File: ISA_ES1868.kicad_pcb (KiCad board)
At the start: 4 copper layers, 104.1 x 99.1 mm, 105 parts, among them J1 LINE IN, J10 Volume buttons, J11 ISA BUS, J2 MIC, J3 Joystick/MIDI, J5 Wavetable, J7 SPKR OUT, J8 LINE OUT, U1 L78L05, U2 74LS138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

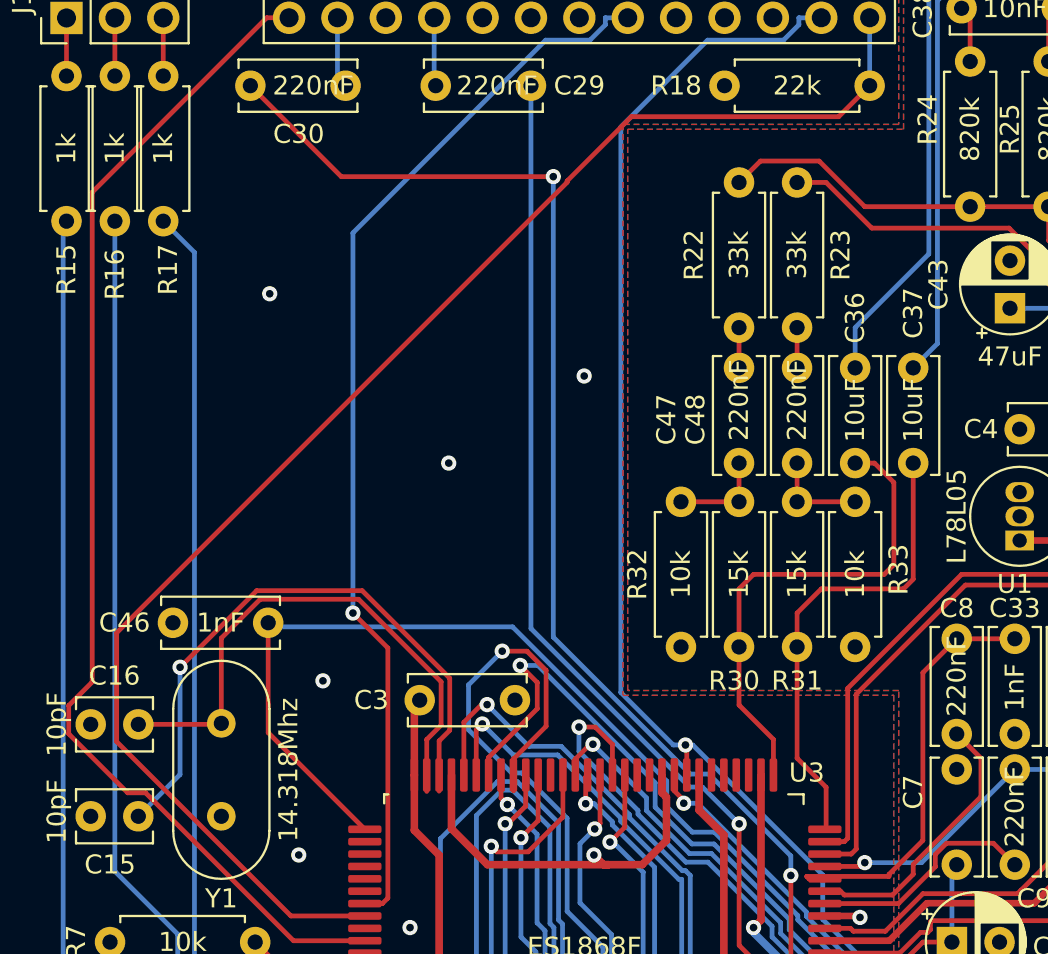
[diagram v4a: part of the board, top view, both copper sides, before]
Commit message: Changed some routing
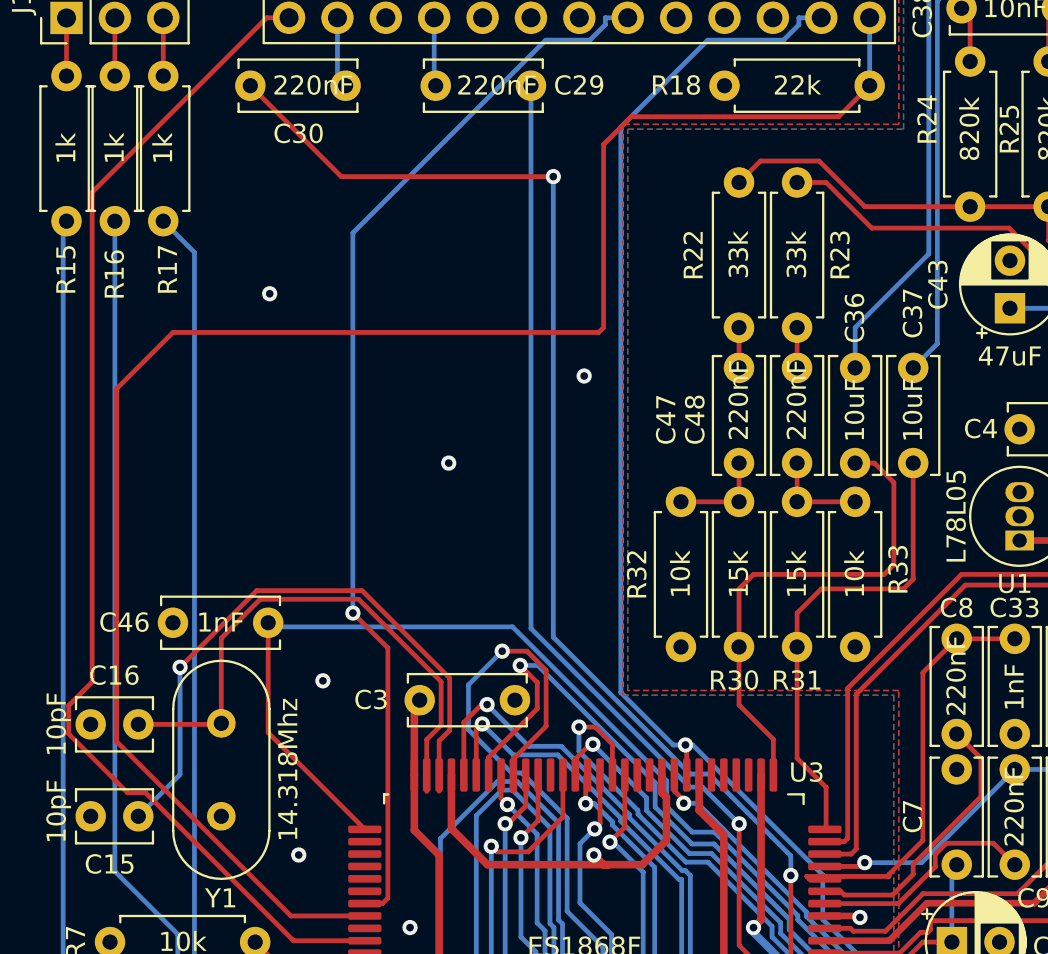
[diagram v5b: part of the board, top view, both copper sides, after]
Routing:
- net /MCLK: track 77.6 -> 90.7 mm
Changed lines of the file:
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@@
     (thickness 1.6)
     (drawings 14)
-    (tracks 1333)
+    (tracks 1336)
     (zones 0)
     (modules 105)
@@
     (tags "solder jumper open")
     (attr virtual)
-    (fp_text reference JP6 (at 0 -2.032 270) (layer B.SilkS)
+    (fp_text reference JP6 (at -2.27 0.254 180) (layer B.SilkS)
       (effects (font (size 1 1) (thickness 0.15)) (justify mirror))
     )
@@
     (tags "solder jumper open")
     (attr virtual)
-    (fp_text reference JP4 (at 0 1.778 270) (layer B.SilkS)
+    (fp_text reference JP4 (at -2.27 0 180) (layer B.SilkS)
       (effects (font (size 1 1) (thickness 0.15)) (justify mirror))
     )
@@
     (descr "C, Disc series, Radial, pin pitch=5.00mm, , diameter*width=6*2.5mm^2, Capacitor, http://cdn-reichelt.de/documents/datenblatt/B300/DS_KERKO_TC.pdf")
     (tags "C Disc series Radial pin pitch 5.00mm  diameter 6mm width 2.5mm Capacitor")
-    (fp_text reference C7 (at 3.81 -2.286 90) (layer F.SilkS)
+    (fp_text reference C7 (at 2.54 -2.286 90) (layer F.SilkS)
       (effects (font (size 1 1) (thickness 0.15)))
     )
@@
   (segment (start 254.508 108.956) (end 253.3327 108.956) (width 0.25) (layer B.Cu) (net 54))
   (via (at 247.377 147.1322) (size 0.8) (layers F.Cu B.Cu) (net 54))
-  (segment (start 230.545 156.109) (end 226.6705 156.109) (width 0.25) (layer F.Cu) (net 55))
-  (segment (start 226.6705 156.109) (end 217.518 146.9565) (width 0.25) (layer F.Cu) (net 55))
-  (segment (start 217.518 146.9565) (end 217.518 141.2428) (width 0.25) (layer F.Cu) (net 55))
-  (segment (start 217.518 141.2428) (end 241.1651 117.5957) (width 0.25) (layer F.Cu) (net 55))
-  (segment (start 241.1651 117.5957) (end 241.1651 117.5247) (width 0.25) (layer F.Cu) (net 55))
-  (segment (start 241.1651 117.5247) (end 244.5423 114.1475) (width 0.25) (layer F.Cu) (net 55))
   (segment (start 244.5423 114.1475) (end 255.4225 114.1475) (width 0.25) (layer F.Cu) (net 55))
   (segment (start 255.4225 114.1475) (end 257.048 112.522) (width 0.25) (layer F.Cu) (net 55))
   (segment (start 257.048 108.956) (end 257.048 112.522) (width 0.25) (layer B.Cu) (net 55))
+  (segment (start 243.078 115.6118) (end 243.0989 115.5909) (width 0.25) (layer F.Cu) (net 55))
+  (segment (start 243.078 125.222) (end 243.078 115.6118) (width 0.25) (layer F.Cu) (net 55))
+  (segment (start 242.824 125.476) (end 243.078 125.222) (width 0.25) (layer F.Cu) (net 55))
+  (segment (start 220.472 125.476) (end 242.824 125.476) (width 0.25) (layer F.Cu) (net 55))
+  (segment (start 217.518 128.43) (end 220.472 125.476) (width 0.25) (layer F.Cu) (net 55))
+  (segment (start 226.6705 156.109) (end 217.518 146.9565) (width 0.25) (layer F.Cu) (net 55))
+  (segment (start 230.545 156.109) (end 226.6705 156.109) (width 0.25) (layer F.Cu) (net 55))
+  (segment (start 217.518 146.9565) (end 217.518 128.43) (width 0.25) (layer F.Cu) (net 55))
+  (segment (start 243.0989 115.5909) (end 244.5423 114.1475) (width 0.25) (layer F.Cu) (net 55))
   (segment (start 219.964 108.966) (end 219.964 112.014) (width 0.25) (layer F.Cu) (net 56))
   (segment (start 217.424 108.966) (end 217.424 112.014) (width 0.25) (layer F.Cu) (net 57))

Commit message: Change silkscreen
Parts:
- J10: value Volume buttons -> Vol. Btns
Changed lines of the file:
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@@
   (page A3)
   (layers
-    (0 F.Cu signal)
-    (1 In1.Cu power)
-    (2 In2.Cu power)
-    (31 B.Cu signal)
+    (0 F.Cu signal hide)
+    (1 In1.Cu power hide)
+    (2 In2.Cu power hide)
+    (31 B.Cu signal hide)
     (32 B.Adhes user)
     (33 F.Adhes user)
@@
       (effects (font (size 1 1) (thickness 0.15)))
     )
-    (fp_text value "LINE OUT" (at 4.385 7.35 90) (layer F.Fab)
+    (fp_text value "LINE OUT" (at -2.6 2.54) (layer F.SilkS)
       (effects (font (size 1 1) (thickness 0.15)))
     )
@@
       (effects (font (size 1 1) (thickness 0.15)))
     )
-    (fp_text value 100nF (at 2.5 2.5) (layer F.Fab)
+    (fp_text value 100nF (at 3.048 0) (layer F.SilkS)
       (effects (font (size 1 1) (thickness 0.15)))
     )
@@
     (descr "Resistor, Axial_DIN0207 series, Axial, Horizontal, pin pitch=7.62mm, 0.25W = 1/4W, length*diameter=6.3*2.5mm^2, http://cdn-reichelt.de/documents/datenblatt/B400/1_4W%23YAG.pdf")
     (tags "Resistor Axial_DIN0207 series Axial Horizontal pin pitch 7.62mm 0.25W = 1/4W length 6.3mm diameter 2.5mm")
-    (fp_text reference R18 (at 10.16 0) (layer F.SilkS)
+    (fp_text reference R18 (at 4.064 -2.286) (layer F.SilkS)
       (effects (font (size 1 1) (thickness 0.15)))
     )
@@
       (effects (font (size 1 1) (thickness 0.15)))
     )
-    (fp_text value "Volume buttons" (at 1.27 7.41 90) (layer F.Fab)
+    (fp_text value "Vol. Btns" (at 1.27 7.41 90) (layer F.SilkS)
       (effects (font (size 1 1) (thickness 0.15)))
     )
@@
       (effects (font (size 1 1) (thickness 0.15)))
     )
-    (fp_text value Wavetable (at 1.27 32.81 90) (layer F.Fab)
+    (fp_text value Wavetable (at 5.344 12.446) (layer F.SilkS)
       (effects (font (size 1 1) (thickness 0.15)))
     )
@@
       (effects (font (size 1 1) (thickness 0.15)))
     )
-    (fp_text value Joystick/MIDI (at -9.695 15.85 90) (layer F.Fab)
+    (fp_text value Joystick/MIDI (at -10.668 6.096 90) (layer F.SilkS)
       (effects (font (size 1 1) (thickness 0.15)))
     )
@@
     (descr "CP, Radial series, Radial, pin pitch=2.50mm, , diameter=5mm, Electrolytic Capacitor")
     (tags "CP Radial series Radial pin pitch 2.50mm  diameter 5mm Electrolytic Capacitor")
-    (fp_text reference C43 (at 1.25 -3.75 90) (layer F.SilkS)
+    (fp_text reference C43 (at 3.302 -4.064) (layer F.SilkS)
       (effects (font (size 1 1) (thickness 0.15)))
     )
@@
       (effects (font (size 1 1) (thickness 0.15)))
     )
-    (fp_text value 100nF (at 2.5 2.5 90) (layer F.Fab)
+    (fp_text value 100nF (at 3.048 0 90) (layer F.SilkS)
       (effects (font (size 1 1) (thickness 0.15)))
     )
@@
       (effects (font (size 1 1) (thickness 0.15)))
     )
-    (fp_text value 100nF (at 2.5 2.5 90) (layer F.Fab)
+    (fp_text value 100nF (at 1.778 0 90) (layer F.SilkS)
       (effects (font (size 1 1) (thickness 0.15)))
     )
@@
     (descr "C, Disc series, Radial, pin pitch=5.00mm, , diameter*width=6*2.5mm^2, Capacitor, http://cdn-reichelt.de/documents/datenblatt/B300/DS_KERKO_TC.pdf")
     (tags "C Disc series Radial pin pitch 5.00mm  diameter 6mm width 2.5mm Capacitor")
-    (fp_text reference C29 (at -2.54 0) (layer F.SilkS)
+    (fp_text reference C29 (at 2.794 -2.54) (layer F.SilkS)
       (effects (font (size 1 1) (thickness 0.15)))
     )
@@
       (effects (font (size 1 1) (thickness 0.15)))
     )
-    (fp_text value 100nF (at 2.5 2.5) (layer F.Fab)
+    (fp_text value 100nF (at 1.952 0) (layer F.SilkS)
       (effects (font (size 1 1) (thickness 0.15)))
     )
@@
       (effects (font (size 1 1) (thickness 0.15)))
     )
-    (fp_text value 100nF (at 2.5 2.5 90) (layer F.Fab)
+    (fp_text value 100nF (at 1.952 0 90) (layer F.SilkS)
       (effects (font (size 1 1) (thickness 0.15)))
     )
@@
       (effects (font (size 1 1) (thickness 0.15)))
     )
-    (fp_text value 100nF (at 2.5 2.5 90) (layer F.Fab)
+    (fp_text value 100nF (at 3.048 0 90) (layer F.SilkS)
       (effects (font (size 1 1) (thickness 0.15)))
     )
@@
       (effects (font (size 1 1) (thickness 0.15)))
     )
-    (fp_text value 100nF (at 2.5 2.5 90) (layer F.Fab)
+    (fp_text value 100nF (at 3.048 0 90) (layer F.SilkS)
       (effects (font (size 1 1) (thickness 0.15)))
     )
@@
       (effects (font (size 1 1) (thickness 0.15)))
     )
-    (fp_text value 100nF (at 2.5 2.5) (layer F.Fab)
+    (fp_text value 100nF (at 3.048 0) (layer F.SilkS)
       (effects (font (size 1 1) (thickness 0.15)))
     )
@@
       (effects (font (size 1 1) (thickness 0.15)))
     )
-    (fp_text value 100nF (at 2.5 2.5) (layer F.Fab)
+    (fp_text value 100nF (at 3.048 0) (layer F.SilkS)
       (effects (font (size 1 1) (thickness 0.15)))
     )
@@
       (effects (font (size 1 1) (thickness 0.15)))
     )
-    (fp_text value 100nF (at 2.5 2.5 90) (layer F.Fab)
+    (fp_text value 100nF (at 3.048 0 90) (layer F.SilkS)
       (effects (font (size 1 1) (thickness 0.15)))
     )
@@
     (descr "CP, Radial series, Radial, pin pitch=2.50mm, , diameter=5mm, Electrolytic Capacitor")
     (tags "CP Radial series Radial pin pitch 2.50mm  diameter 5mm Electrolytic Capacitor")
-    (fp_text reference C51 (at -3.302 1.016) (layer F.SilkS)
+    (fp_text reference C51 (at -3.048 2.032) (layer F.SilkS)
       (effects (font (size 1 1) (thickness 0.15)))
     )
-    (fp_text value 10uF (at -3.048 2.54) (layer F.SilkS)
+    (fp_text value 10uF (at -3.048 0.508) (layer F.SilkS)
       (effects (font (size 1 1) (thickness 0.15)))
     )
@@
       (effects (font (size 1 1) (thickness 0.15)))
     )
-    (fp_text value 100nF (at 2.5 2.5) (layer F.Fab)
+    (fp_text value 100nF (at 3.302 0) (layer F.SilkS)
       (effects (font (size 1 1) (thickness 0.15)))
     )

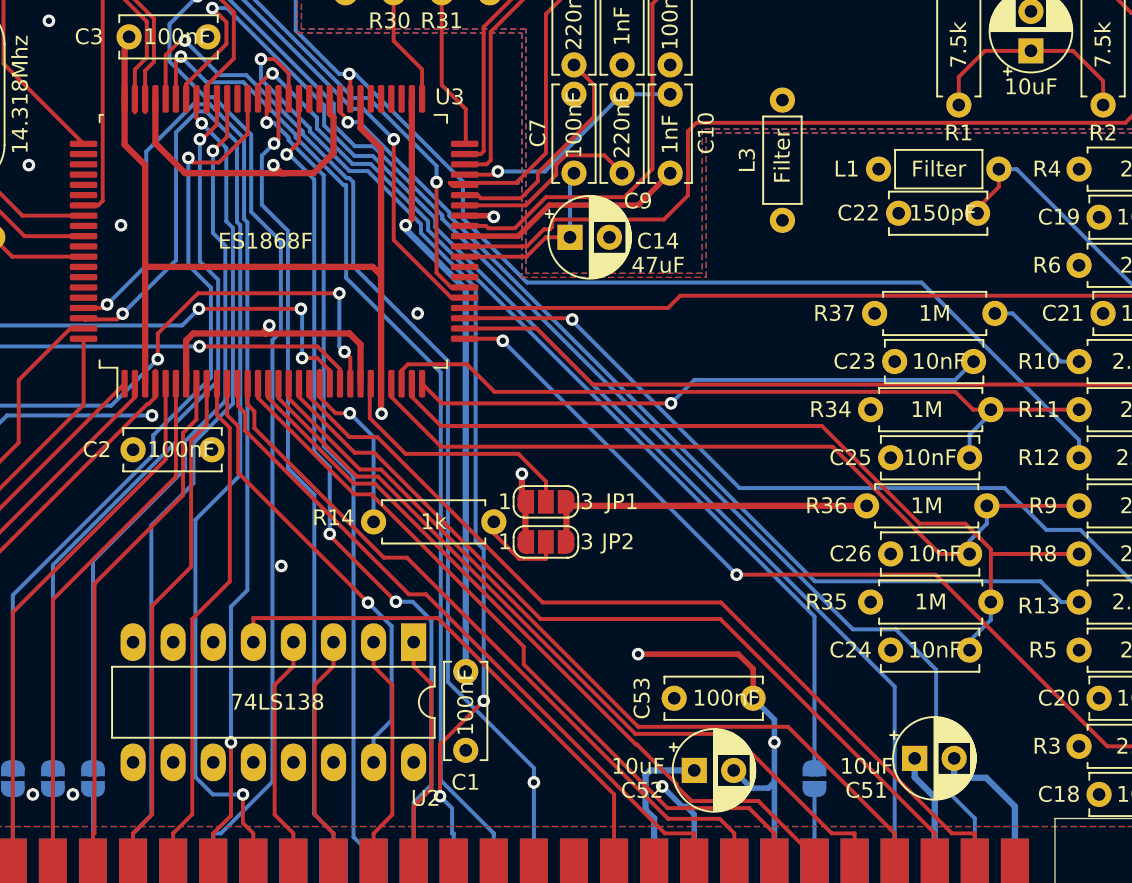
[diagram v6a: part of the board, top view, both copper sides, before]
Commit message: More vias for a better ground plane
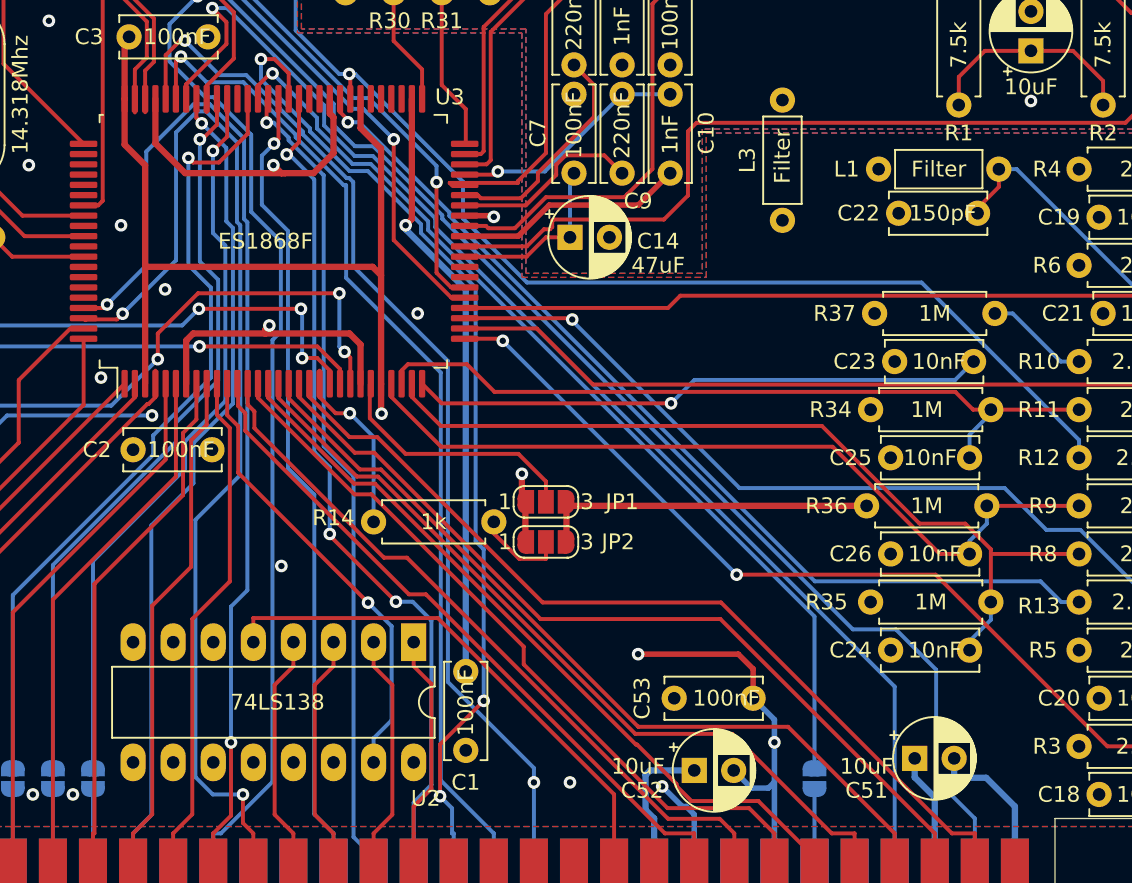
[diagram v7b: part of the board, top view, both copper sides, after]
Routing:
- net GND: track 664.7 -> 685.0 mm, vias 17 -> 20
- net GNDA: track 296.6 -> 303.8 mm, vias 0 -> 1
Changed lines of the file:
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@@
     (thickness 1.6)
     (drawings 14)
-    (tracks 1336)
+    (tracks 1355)
     (zones 0)
     (modules 105)
@@
   (page A3)
   (layers
-    (0 F.Cu signal hide)
-    (1 In1.Cu power hide)
-    (2 In2.Cu power hide)
-    (31 B.Cu signal hide)
+    (0 F.Cu signal)
+    (1 In1.Cu power)
+    (2 In2.Cu power)
+    (31 B.Cu signal)
     (32 B.Adhes user)
     (33 F.Adhes user)
@@
   (segment (start 267.97 188.214) (end 269.24 189.484) (width 0.4) (layer In1.Cu) (net 2))
   (segment (start 269.24 189.484) (end 269.24 191.262) (width 0.4) (layer In1.Cu) (net 2))
-  (segment (start 254.762 184.992) (end 266.272 184.992) (width 0.4) (layer In1.Cu) (net 2))
   (segment (start 266.272 184.992) (end 267.97 186.69) (width 0.4) (layer In1.Cu) (net 2))
   (segment (start 233.68 173.99) (end 233.68 183.134) (width 0.4) (layer In1.Cu) (net 2))
@@
   (segment (start 229.108 152.908) (end 232.918 156.718) (width 0.4) (layer In1.Cu) (net 2))
   (segment (start 227.076 152.908) (end 229.108 152.908) (width 0.4) (layer In1.Cu) (net 2))
-  (segment (start 232.918 156.718) (end 242.316 156.718) (width 0.4) (layer In1.Cu) (net 2))
   (segment (start 242.316 156.718) (end 242.316 153.162) (width 0.4) (layer In1.Cu) (net 2))
   (segment (start 242.316 163.068) (end 242.316 156.718) (width 0.4) (layer In1.Cu) (net 2))
@@
   (segment (start 251.714 157.48) (end 250.952 156.718) (width 0.4) (layer In1.Cu) (net 2))
   (segment (start 251.714 162.306) (end 251.714 157.48) (width 0.4) (layer In1.Cu) (net 2))
+  (via (at 261.366 192.024) (size 0.8) (drill 0.4) (layers F.Cu B.Cu) (net 2))
+  (segment (start 261.366 185.834) (end 260.524 184.992) (width 0.4) (layer In1.Cu) (net 2))
+  (segment (start 261.366 192.024) (end 261.366 185.834) (width 0.4) (layer In1.Cu) (net 2))
+  (segment (start 260.524 184.992) (end 266.272 184.992) (width 0.4) (layer In1.Cu) (net 2))
+  (segment (start 254.762 184.992) (end 260.524 184.992) (width 0.4) (layer In1.Cu) (net 2))
+  (via (at 235.712 160.782) (size 0.8) (drill 0.4) (layers F.Cu B.Cu) (net 2))
+  (segment (start 235.712 156.972) (end 235.458 156.718) (width 0.4) (layer In1.Cu) (net 2))
+  (segment (start 235.712 160.782) (end 235.712 156.972) (width 0.4) (layer In1.Cu) (net 2))
+  (segment (start 235.458 156.718) (end 242.316 156.718) (width 0.4) (layer In1.Cu) (net 2))
+  (segment (start 232.918 156.718) (end 235.458 156.718) (width 0.4) (layer In1.Cu) (net 2))
+  (via (at 231.648 166.37) (size 0.8) (drill 0.4) (layers F.Cu B.Cu) (net 2))
+  (segment (start 235.712 163.576) (end 235.712 160.782) (width 0.4) (layer In1.Cu) (net 2))
+  (segment (start 235.204 164.084) (end 235.712 163.576) (width 0.4) (layer In1.Cu) (net 2))
+  (segment (start 232.664 164.084) (end 235.204 164.084) (width 0.4) (layer In1.Cu) (net 2))
+  (segment (start 231.648 165.1) (end 232.664 164.084) (width 0.4) (layer In1.Cu) (net 2))
+  (segment (start 231.648 166.37) (end 231.648 165.1) (width 0.4) (layer In1.Cu) (net 2))
   (segment (start 239.738 111.252) (end 239.024 111.252) (width 0.35) (layer In2.Cu) (net 3))
   (segment (start 239.024 111.252) (end 236.728 108.956) (width 0.35) (layer In2.Cu) (net 3))
@@
   (segment (start 226.568 106.416) (end 229.108 106.416) (width 0.35) (layer In1.Cu) (net 5))
   (segment (start 229.108 106.416) (end 231.648 106.416) (width 0.35) (layer In1.Cu) (net 5))
+  (via (at 290.576 148.844) (size 0.8) (drill 0.4) (layers F.Cu B.Cu) (net 5))
+  (segment (start 290.576 148.844) (end 290.576 147.828) (width 0.35) (layer In1.Cu) (net 5))
+  (segment (start 290.576 147.828) (end 292.354 146.05) (width 0.35) (layer In1.Cu) (net 5))
+  (segment (start 292.354 144.944) (end 290.576 143.166) (width 0.35) (layer In1.Cu) (net 5))
+  (segment (start 292.354 146.05) (end 292.354 144.944) (width 0.35) (layer In1.Cu) (net 5))
   (segment (start 295.148 141.478) (end 296.926 143.256) (width 0.25) (layer F.Cu) (net 6))
   (segment (start 296.926 143.256) (end 300.054 143.256) (width 0.25) (layer F.Cu) (net 6))
